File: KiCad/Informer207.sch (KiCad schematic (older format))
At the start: 24 parts, among them J1 PROG, J2 USB_B_Micro, J3 RS232, SW1 RESET, SW2 BOOT, U1 ESP32-WROOM-32, U2 MAX3232, U3 AMS1117-3.3

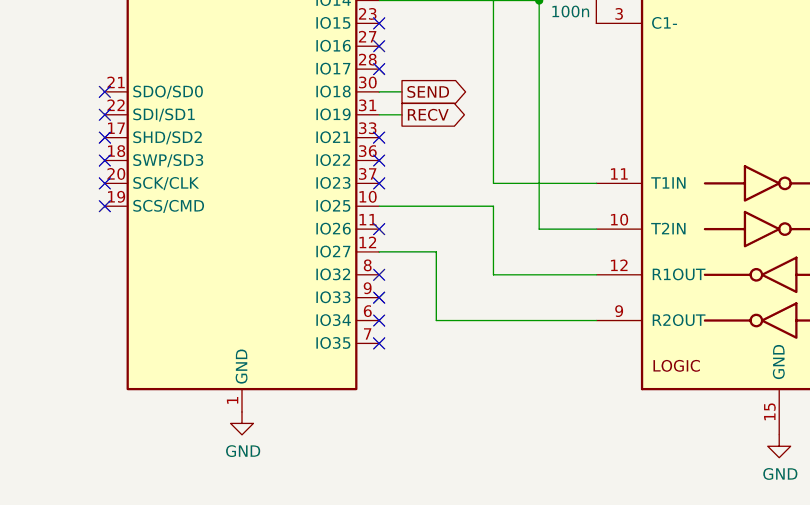
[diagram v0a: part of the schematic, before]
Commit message: Added possible Ready To Recieve line (some activity on it)
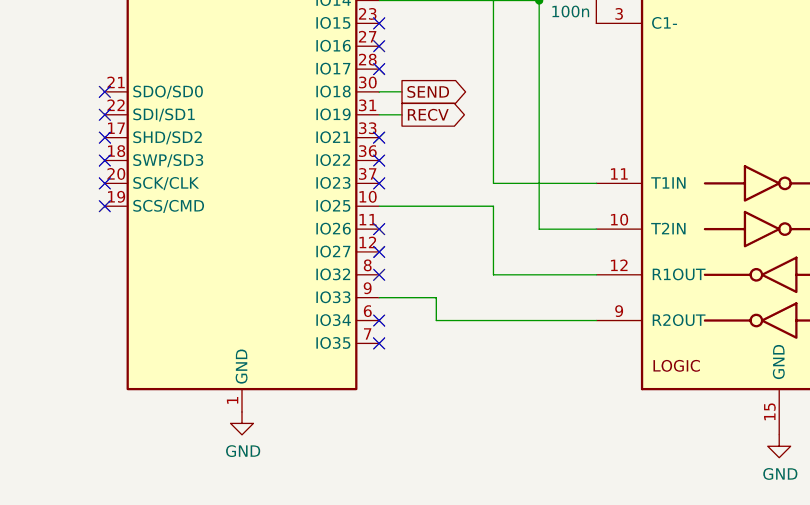
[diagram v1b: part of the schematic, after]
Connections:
- net at U2.9 (R2OUT): now also U1.9 (IO33); no longer U1.12 (IO27)
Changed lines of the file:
@@
 	2350 1800 2200 1800
 Connection ~ 2200 1800
-Wire Wire Line
-	3550 3700 3800 3700
-Wire Wire Line
-	3800 3700 3800 4000
 $Comp
 L Device:R R3
@@
 NoConn ~ 3550 3600
 NoConn ~ 3550 3800
-NoConn ~ 3550 3900
+NoConn ~ 3550 3700
 NoConn ~ 3550 4000
 NoConn ~ 3550 4100
@@
 	7700 1350 7600 1350
 Connection ~ 7600 1350
+Wire Wire Line
+	3550 3900 3800 3900
+Wire Wire Line
+	3800 3900 3800 4000
 $EndSCHEMATC
